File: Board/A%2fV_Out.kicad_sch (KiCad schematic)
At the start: 30 parts, among them IC2 74245DW, X1 1503_09, X2 D-SUB15-HDR15RA

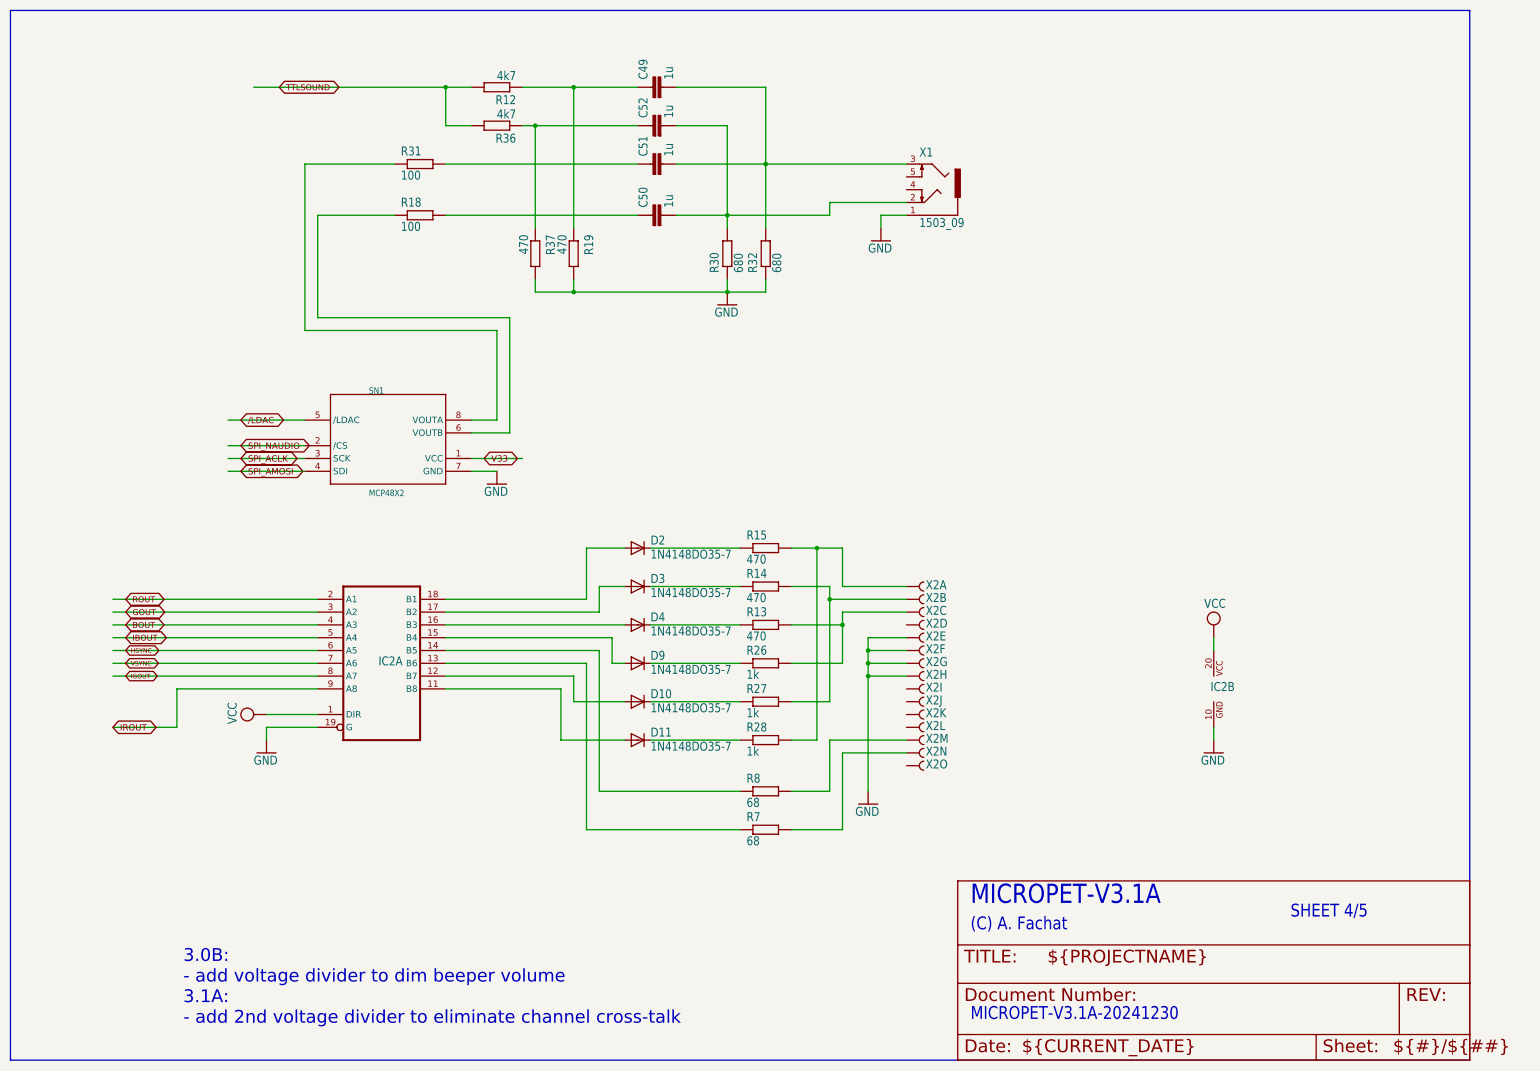
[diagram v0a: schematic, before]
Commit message: final touches, 22u audio output caps
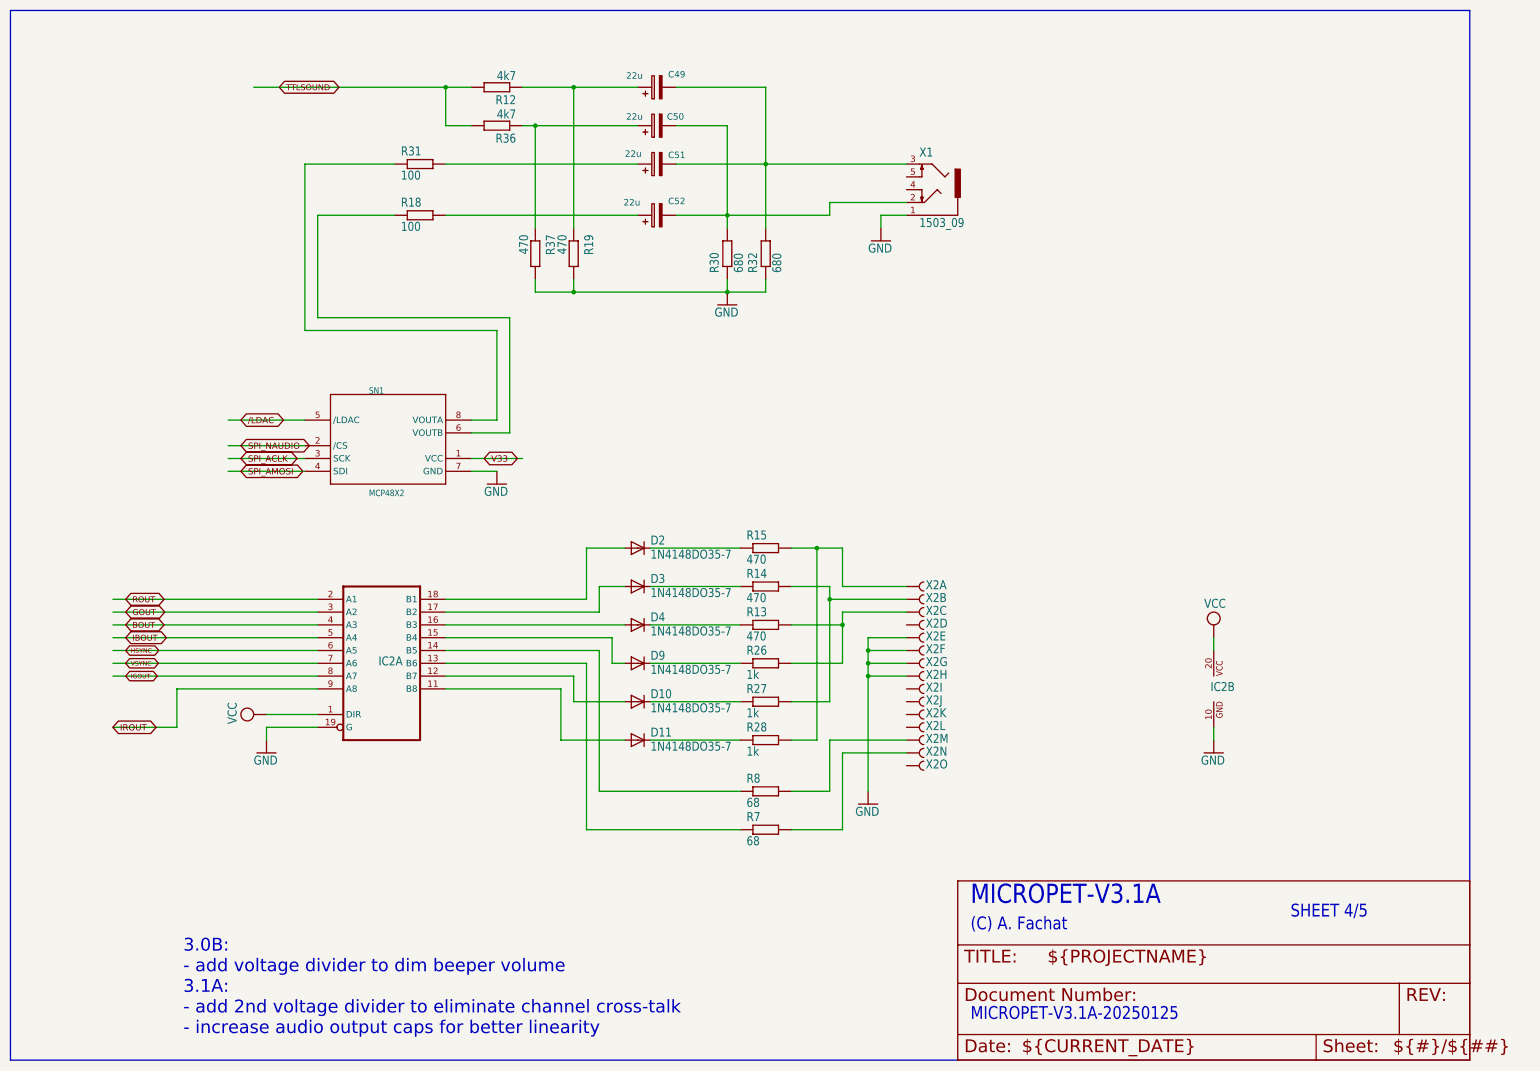
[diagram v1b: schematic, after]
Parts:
- removed C49, C50, C51, C52: 1u, micropet_v3:C050-025X075, symbol micropet_v3-eagle-import:C-EU050-025X075
- added C49, C50, C51, C52: 22u, Capacitor_THT:CP_Radial_D5.0mm_P2.50mm, symbol Device:C_Polarized
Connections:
- net at R18.2: now also C52.1
- net at R36.1, R37.1: now also C50.1
- net at R31.2: now also C51.1
- net at R32.2, X1.3: now also C49.2, C51.2
- net at R30.2, X1.2: now also C50.2, C52.2
- net at R12.1, R19.1: now also C49.1
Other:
- note added: "3.0B: - add voltage divider to dim beeper volume 3.1A: - add 2nd voltage divider to eliminate channel cross-talk - increase audio output caps for better linearity"
- note added: "MICROPET-V3.1A-20250125"
- note removed: "3.0B: - add voltage divider to dim beeper volume 3.1A: - add 2nd voltage divider to eliminate channel cross-talk"
- note removed: "MICROPET-V3.1A-20241230"
